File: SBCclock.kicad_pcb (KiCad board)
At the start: 2 copper layers, 37.5 x 23.4 mm, 12 parts, among them J1 Conn_01x06_Male, J2 Conn_01x06_Male, U1 74HCT04, U2 74HC163, U3 74AHC1G02, Y1 25.175MHz

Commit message: chore: tweak values
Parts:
- C2: value 18pF -> 1uF
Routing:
- net Clock6: track 34.2 -> 31.4 mm

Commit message: chore: adjust routing
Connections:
- J2 pad 4: unconnected-(J2-Pin_4-Pad4) -> ~{RESET}
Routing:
- net GND: track 88.7 -> 89.4 mm
- added copper zone on F.Cu, net GND
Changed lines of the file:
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@@
   (net 13 "unconnected-(U1-Pad13)")
   (net 14 "Net-(C1-Pad2)")
-  (net 15 "unconnected-(J2-Pin_4-Pad4)")
+  (net 15 "~{RESET}")
   (net 16 "Net-(U2-CEP)")
   (net 17 "unconnected-(U2-D0-Pad3)")
@@
       (net 9 "~{E}") (pinfunction "Pin_3") (pintype "passive"))
     (pad "4" thru_hole oval (at 0 -7.62 180) (size 1.7 1.7) (drill 1) (layers "*.Cu" "*.Mask")
-      (net 15 "unconnected-(J2-Pin_4-Pad4)") (pinfunction "Pin_4") (pintype "passive+no_connect"))
+      (net 15 "~{RESET}") (pinfunction "Pin_4") (pintype "passive"))
     (pad "5" thru_hole oval (at 0 -10.16 180) (size 1.7 1.7) (drill 1) (layers "*.Cu" "*.Mask")
       (net 6 "Clock3") (pinfunction "Pin_5") (pintype "passive"))
@@
     (style (thickness 0.15) (arrow_length 1.27) (text_position_mode 0) (extension_height 0.58642) (extension_offset 0.5) keep_text_aligned)
   )
+  (dimension (type aligned) (layer "User.2")
+    (pts (xy 143.002 83.3628) (xy 143.002 59.9948))
+    (height -4.4196)
+    (gr_text "23.3680 mm" (at 137.4324 71.6788 90) (layer "User.2")
+      (effects (font (size 1 1) (thickness 0.15)))
+    )
+    (format (prefix "") (suffix "") (units 3) (units_format 1) (precision 4))
+    (style (thickness 0.15) (arrow_length 1.27) (text_position_mode 0) (extension_height 0.58642) (extension_offset 0.5) keep_text_aligned)
+  )
+  (dimension (type aligned) (layer "User.2")
+    (pts (xy 143.002 83.3628) (xy 180.4924 83.3628))
+    (height 3.9116)
+    (gr_text "37.4904 mm" (at 161.7472 86.1244) (layer "User.2")
+      (effects (font (size 1 1) (thickness 0.15)))
+    )
+    (format (prefix "") (suffix "") (units 3) (units_format 1) (precision 4))
+    (style (thickness 0.15) (arrow_length 1.27) (text_position_mode 0) (extension_height 0.58642) (extension_offset 0.5) keep_text_aligned)
+  )
+  (segment (start 156.413 75.7428) (end 156.515 75.7428) (width 0.5) (layer "F.Cu") (net 1))
+  (segment (start 153.304 78.5472) (end 151.9012 78.5472) (width 0.5) (layer "F.Cu") (net 1))
+  (segment (start 177.343 61.3664) (end 167.0812 61.3664) (width 0.5) (layer "F.Cu") (net 1))
+  (segment (start 147.828 63.8048) (end 146.58 63.8048) (width 0.5) (layer "F.Cu") (net 1))
   (segment (start 178.41 68.58) (end 178.41 62.4332) (width 0.5) (layer "F.Cu") (net 1))
-  (segment (start 156.413 75.7428) (end 156.515 75.7428) (width 0.5) (layer "F.Cu") (net 1))
+  (segment (start 178.41 62.4332) (end 177.343 61.3664) (width 0.5) (layer "F.Cu") (net 1))
   (segment (start 156.7688 68.072) (end 159.071 65.7698) (width 0.5) (layer "F.Cu") (net 1))
-  (segment (start 153.304 78.5472) (end 151.9012 78.5472) (width 0.5) (layer "F.Cu") (net 1))
-  (segment (start 147.828 63.8048) (end 146.58 63.8048) (width 0.5) (layer "F.Cu") (net 1))
-  (segment (start 155.956 72.2884) (end 156.7688 71.4756) (width 0.5) (layer "F.Cu") (net 1))
-  (segment (start 168.266 61.3664) (end 166.894 62.738) (width 0.5) (layer "F.Cu") (net 1))
-  (segment (start 177.343 61.3664) (end 168.266 61.3664) (width 0.5) (layer "F.Cu") (net 1))
   (segment (start 155.956 72.2884) (end 155.891 72.2234) (width 0.5) (layer "F.Cu") (net 1))
   (segment (start 156.515 75.7428) (end 156.529 75.757) (width 0.5) (layer "F.Cu") (net 1))
-  (segment (start 178.41 62.4332) (end 177.343 61.3664) (width 0.5) (layer "F.Cu") (net 1))
-  (segment (start 159.071 65.7698) (end 163.8622 65.7698) (width 0.5) (layer "F.Cu") (net 1))
-  (segment (start 163.8622 65.7698) (end 166.894 62.738) (width 0.5) (layer "F.Cu") (net 1))
+  (segment (start 167.0812 61.3664) (end 166.894 61.5536) (width 0.5) (layer "F.Cu") (net 1))
   (segment (start 157.226 75.757) (end 156.602 75.757) (width 0.5) (layer "F.Cu") (net 1))
+  (segment (start 155.956 72.2884) (end 156.7688 71.4756) (width 0.5) (layer "F.Cu") (net 1))
+  (segment (start 166.894 61.5536) (end 166.894 62.738) (width 0.5) (layer "F.Cu") (net 1))
+  (segment (start 159.071 65.7698) (end 162.7794 65.7698) (width 0.5) (layer "F.Cu") (net 1))
   (segment (start 156.7688 71.4756) (end 156.7688 68.072) (width 0.5) (layer "F.Cu") (net 1))
+  (segment (start 165.8112 62.738) (end 166.894 62.738) (width 0.5) (layer "F.Cu") (net 1))
   (segment (start 153.314 78.5368) (end 153.304 78.5472) (width 0.5) (layer "F.Cu") (net 1))
   (segment (start 156.529 75.757) (end 156.602 75.757) (width 0.5) (layer "F.Cu") (net 1))
+  (segment (start 162.7794 65.7698) (end 165.8112 62.738) (width 0.5) (layer "F.Cu") (net 1))
   (segment (start 156.602 75.757) (end 157.226 75.757) (width 0.5) (layer "F.Cu") (net 1))
   (segment (start 155.891 72.2234) (end 154.9146 72.2234) (width 0.5) (layer "F.Cu") (net 1))
@@
     )
   )
-  (zone (net 1) (net_name "GND") (layer "B.Cu") (hatch edge 0.508)
+  (zone (net 1) (net_name "GND") (layers "F&B.Cu") (hatch edge 0.508)
     (connect_pads (clearance 0.508))
     (min_thickness 0.254) (filled_areas_thickness no)

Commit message: revise E generation
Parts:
- added C3: 1uF, Capacitor_SMD:C_0805_2012Metric_Pad1.18x1.45mm_HandSolder, F.Cu at (163.5, 81.1)
- added D1: LED, LED_SMD:LED_0805_2012Metric_Pad1.15x1.40mm_HandSolder, F.Cu at (145.8, 81.0)
- added R5: 330R, Resistor_SMD:R_0805_2012Metric_Pad1.20x1.40mm_HandSolder, F.Cu at (145.8, 78.9)
- added U4: 74AHC1G08, Package_TO_SOT_SMD:SOT-353_SC-70-5_Handsoldering, F.Cu at (156.3, 79.2)
- added U5: 74AHC1G32, Package_TO_SOT_SMD:SOT-353_SC-70-5_Handsoldering, F.Cu at (159.1, 73.9)
- moved U1 9.91 mm to (170.9, 78.6)
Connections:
- U1 pad 1: Net-(C1-Pad2) -> Net-(R3-Pad1)
- U1 pad 2: Net-(R2-Pad2) -> Net-(C1-Pad1)
- U1 pad 3: Net-(R3-Pad1) -> Net-(C1-Pad2)
- U1 pad 4: Net-(C1-Pad1) -> Net-(R2-Pad2)
- U3 pad 4: E -> Net-(U3-Pad4)
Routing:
- net GND: track 89.4 -> 116.7 mm, vias 4 -> 8
- net +5V: track 47.8 -> 72.4 mm
- net Net-(U3-Pad4): track 0.00 -> 11.9 mm
- net Clock24: track 30.3 -> 41.7 mm, vias 1 -> 5
- net Net-(C1-Pad2): track 28.2 -> 39.0 mm, vias 0 -> 2
- net ~{Q}: track 20.0 -> 9.48 mm
- net ~{E}: track 35.1 -> 24.9 mm
- net Net-(U4-Pad4): track 0.00 -> 7.72 mm
- net Net-(R3-Pad1): track 20.8 -> 13.6 mm, vias 2 -> 0
- net Clock3: track 57.5 -> 64.1 mm, vias 2 -> 3
- net E: track 35.6 -> 29.2 mm, vias 0 -> 1
- net Net-(R2-Pad2): track 10.7 -> 16.2 mm
- net Net-(C1-Pad1): track 30.5 -> 25.4 mm, vias 0 -> 3
- net Clock6: track 31.4 -> 34.7 mm
- net Net-(D1-A): track 0.00 -> 2.14 mm

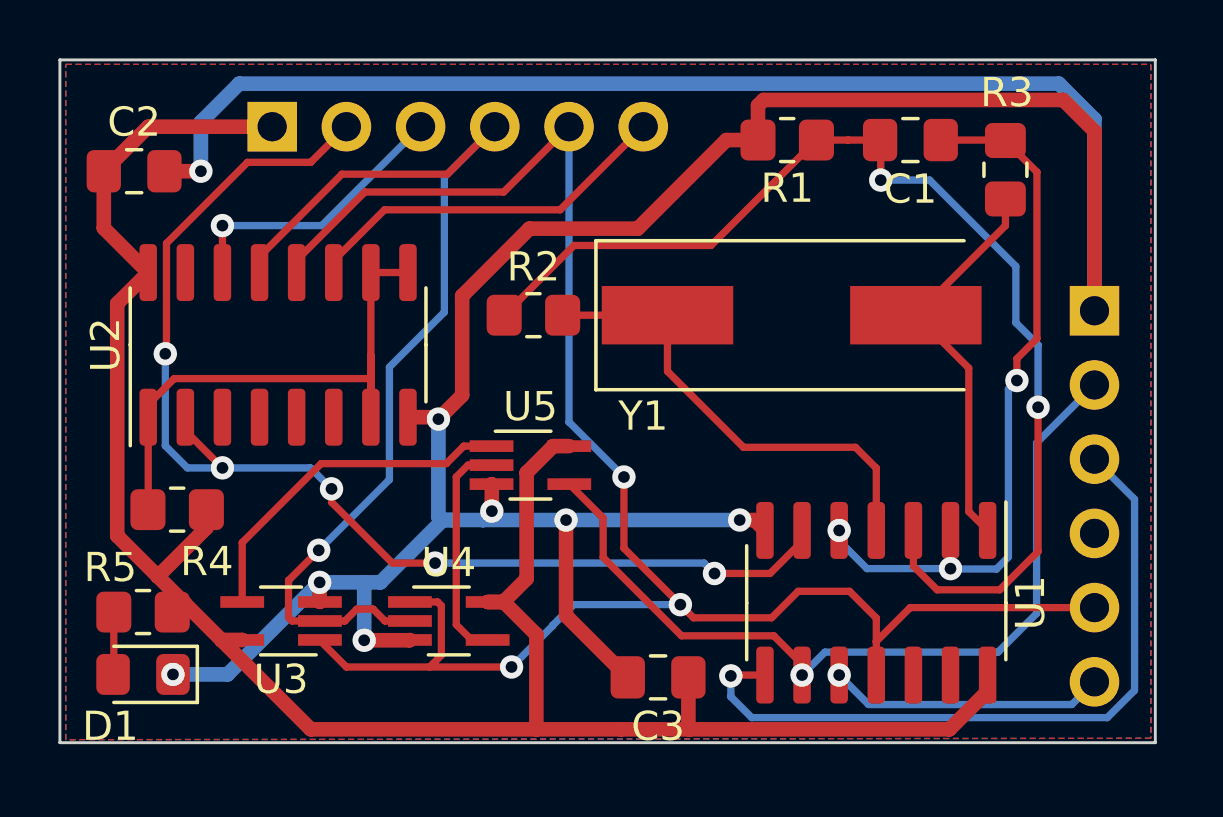
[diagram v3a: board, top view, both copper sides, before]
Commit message: simplified board
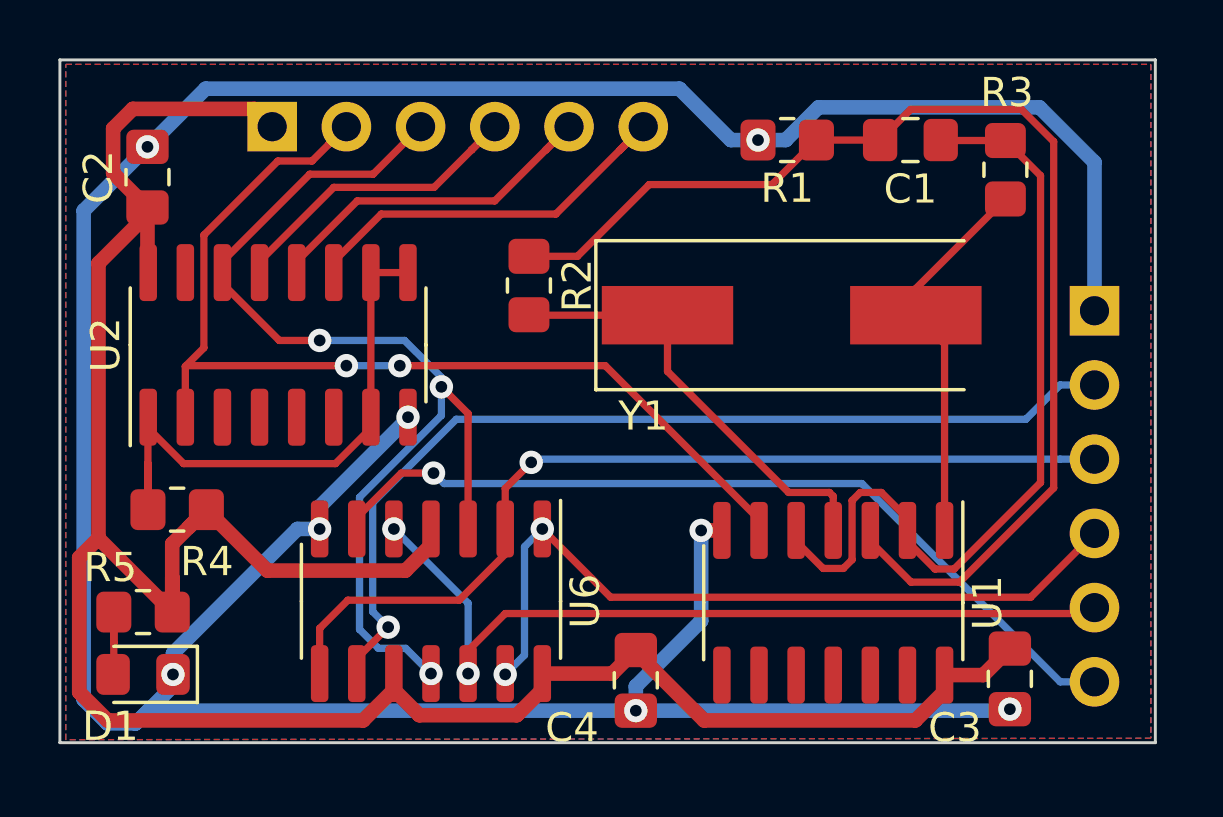
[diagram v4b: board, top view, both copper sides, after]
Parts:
- removed U3: 74AHC1G02, Package_TO_SOT_SMD:SOT-353_SC-70-5_Handsoldering
- removed U4: 74AHC1G08, Package_TO_SOT_SMD:SOT-353_SC-70-5_Handsoldering
- removed U5: 74AHC1G32, Package_TO_SOT_SMD:SOT-353_SC-70-5_Handsoldering
- added C4: 1uF, Capacitor_SMD:C_0805_2012Metric_Pad1.18x1.45mm_HandSolder, F.Cu at (162.7, 81.2)
- added U6: 74HC74, Package_SO:SOIC-14_3.9x8.7mm_P1.27mm, F.Cu at (155.7, 78.5)
- moved C3 12.0 mm to (175.5, 81.2), turned to -90 degrees
- moved U1 1.47 mm to (169.5, 78.6)
- moved R2 1.03 mm to (159.1, 67.7), turned to -90 degrees
- moved C2 0.50 mm to (146.0, 64.0), turned to 90 degrees
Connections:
- J2 pad 5: Clock3 -> Q
- U1 pad 10: ~{Q} -> unconnected-(U1-Pad10)
- U1 pad 11: Clock3 -> unconnected-(U1-Pad11)
- U1 pad 8: ~{E} -> unconnected-(U1-Pad8)
- U1 pad 9: E -> unconnected-(U1-Pad9)
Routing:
- net Clock3: track 64.1 -> 12.9 mm, vias 3 -> 0
- net Q: track 0.00 -> 28.8 mm, vias 0 -> 2
- net Clock12: track 9.79 -> 36.4 mm, vias 1 -> 3
- net ~{RESET}: track 0.00 -> 26.3 mm, vias 0 -> 2
- net Clock6: track 34.7 -> 11.7 mm, vias 1 -> 0
- net ~{Q}: track 9.48 -> 29.2 mm
- net +5V: track 72.4 -> 85.3 mm
- net Net-(U3-Pad4): track 11.9 -> 0.00 mm
- net Net-(U4-Pad4): track 7.72 -> 0.00 mm
- net ~{E}: track 24.9 -> 31.8 mm
- net Clock24: track 41.7 -> 36.1 mm, vias 5 -> 2
- net E: track 29.2 -> 32.9 mm
- net Net-(C1-Pad1): track 25.4 -> 28.7 mm, vias 3 -> 0
- net Net-(C1-Pad2): track 39.0 -> 41.1 mm, vias 2 -> 0
- net GND: track 116.7 -> 114.9 mm
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
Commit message: prepare for production
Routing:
- net +5V: track 85.3 -> 85.9 mm
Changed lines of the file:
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@@
     (fp_line (start 1 0.625) (end -1 0.625)
       (stroke (width 0.1) (type solid)) (layer "F.Fab"))
-    (pad "1" smd roundrect (at -1 0) (size 1.2 1.4) (layers "F.Cu" "F.Paste" "F.Mask") (roundrect_rratio 0.208333)
+    (pad "1" smd roundrect (at -1 0) (size 1.2 1.4) (layers "F.Cu" "F.Paste" "F.Mask") (roundrect_rratio 0.2083333333)
       (net 26 "Net-(D1-A)") (pintype "passive"))
-    (pad "2" smd roundrect (at 1 0) (size 1.2 1.4) (layers "F.Cu" "F.Paste" "F.Mask") (roundrect_rratio 0.208333)
+    (pad "2" smd roundrect (at 1 0) (size 1.2 1.4) (layers "F.Cu" "F.Paste" "F.Mask") (roundrect_rratio 0.2083333333)
       (net 2 "+5V") (pintype "passive"))
     (model "${KICAD6_3DMODEL_DIR}/Resistor_SMD.3dshapes/R_0805_2012Metric.wrl"
@@
     (fp_line (start 1 0.6) (end 1 -0.6)
       (stroke (width 0.1) (type solid)) (layer "F.Fab"))
-    (pad "1" smd roundrect (at -1.025 0 180) (size 1.15 1.4) (layers "F.Cu" "F.Paste" "F.Mask") (roundrect_rratio 0.217391)
+    (pad "1" smd roundrect (at -1.025 0 180) (size 1.15 1.4) (layers "F.Cu" "F.Paste" "F.Mask") (roundrect_rratio 0.2173913043)
       (net 1 "GND") (pinfunction "K") (pintype "passive"))
-    (pad "2" smd roundrect (at 1.025 0 180) (size 1.15 1.4) (layers "F.Cu" "F.Paste" "F.Mask") (roundrect_rratio 0.217391)
+    (pad "2" smd roundrect (at 1.025 0 180) (size 1.15 1.4) (layers "F.Cu" "F.Paste" "F.Mask") (roundrect_rratio 0.2173913043)
       (net 26 "Net-(D1-A)") (pinfunction "A") (pintype "passive"))
     (model "${KICAD6_3DMODEL_DIR}/LED_SMD.3dshapes/LED_0805_2012Metric.wrl"
@@
     (fp_line (start 1 0.625) (end -1 0.625)
       (stroke (width 0.1) (type solid)) (layer "F.Fab"))
-    (pad "1" smd roundrect (at -1.0375 0 270) (size 1.175 1.45) (layers "F.Cu" "F.Paste" "F.Mask") (roundrect_rratio 0.212766)
+    (pad "1" smd roundrect (at -1.0375 0 270) (size 1.175 1.45) (layers "F.Cu" "F.Paste" "F.Mask") (roundrect_rratio 0.2127659574)
       (net 2 "+5V") (pintype "passive"))
-    (pad "2" smd roundrect (at 1.0375 0 270) (size 1.175 1.45) (layers "F.Cu" "F.Paste" "F.Mask") (roundrect_rratio 0.212766)
+    (pad "2" smd roundrect (at 1.0375 0 270) (size 1.175 1.45) (layers "F.Cu" "F.Paste" "F.Mask") (roundrect_rratio 0.2127659574)
       (net 1 "GND") (pintype "passive"))
     (model "${KICAD6_3DMODEL_DIR}/Capacitor_SMD.3dshapes/C_0805_2012Metric.wrl"
@@
     (fp_line (start 1 0.625) (end -1 0.625)
       (stroke (width 0.1) (type solid)) (layer "F.Fab"))
-    (pad "1" smd roundrect (at -1.0375 0 270) (size 1.175 1.45) (layers "F.Cu" "F.Paste" "F.Mask") (roundrect_rratio 0.212766)
+    (pad "1" smd roundrect (at -1.0375 0 270) (size 1.175 1.45) (layers "F.Cu" "F.Paste" "F.Mask") (roundrect_rratio 0.2127659574)
       (net 2 "+5V") (pintype "passive"))
-    (pad "2" smd roundrect (at 1.0375 0 270) (size 1.175 1.45) (layers "F.Cu" "F.Paste" "F.Mask") (roundrect_rratio 0.212766)
+    (pad "2" smd roundrect (at 1.0375 0 270) (size 1.175 1.45) (layers "F.Cu" "F.Paste" "F.Mask") (roundrect_rratio 0.2127659574)
       (net 1 "GND") (pintype "passive"))
     (model "${KICAD6_3DMODEL_DIR}/Capacitor_SMD.3dshapes/C_0805_2012Metric.wrl"
@@
   (segment (start 145.999 65.0455) (end 145.999 65.1617) (width 0.5) (layer "F.Cu") (net 2))
   (segment (start 173.279 81.6019) (end 173.279 81.0484) (width 0.5) (layer "F.Cu") (net 2))
+  (segment (start 143.6624 75.7078) (end 144.323 76.3684) (width 0.5) (layer "F.Cu") (net 2))
   (segment (start 149.657 61.6712) (end 145.496 61.6712) (width 0.5) (layer "F.Cu") (net 2))
   (segment (start 146.0246 67.2734) (end 146.025 67.2734) (width 0.5) (layer "F.Cu") (net 2))
-  (segment (start 145.999 65.278) (end 144.323 66.9544) (width 0.5) (layer "F.Cu") (net 2))
-  (segment (start 144.323 66.9544) (end 144.323 76.3684) (width 0.5) (layer "F.Cu") (net 2))
   (segment (start 162.712 80.264) (end 165.049 82.6008) (width 0.5) (layer "F.Cu") (net 2))
   (segment (start 154.831 77.4726) (end 155.702 76.6011) (width 0.5) (layer "F.Cu") (net 2))
@@
   (segment (start 146.847 77.724) (end 146.847 76.5556) (width 0.5) (layer "F.Cu") (net 2))
   (segment (start 155.702 76.6011) (end 155.702 76.0476) (width 0.5) (layer "F.Cu") (net 2))
+  (segment (start 145.999 65.278) (end 143.6624 67.6146) (width 0.5) (layer "F.Cu") (net 2))
   (segment (start 147.431 75.9714) (end 148.0152 75.3872) (width 0.5) (layer "F.Cu") (net 2))
   (segment (start 153.382 82.6008) (end 154.432 81.5511) (width 0.5) (layer "F.Cu") (net 2))
@@
   (segment (start 150.2664 62.2808) (end 150.266 62.2808) (width 0.5) (layer "F.Cu") (net 2))
   (segment (start 145.999 67.248) (end 146.025 67.2734) (width 0.5) (layer "F.Cu") (net 2))
+  (segment (start 143.6624 67.6146) (end 143.6624 75.7078) (width 0.5) (layer "F.Cu") (net 2))
   (segment (start 145.999 65.1617) (end 145.999 65.278) (width 0.5) (layer "F.Cu") (net 2))
   (segment (start 145.999 65.1617) (end 145.9992 65.1615) (width 0.5) (layer "F.Cu") (net 2))

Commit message: revise clock signal
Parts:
- removed the R3 at (175.4, 63.8)
- added C2: 22pF, Capacitor_SMD:C_0805_2012Metric_Pad1.18x1.45mm_HandSolder, F.Cu at (172.3, 63.7)
- added D2: LED, LED_SMD:LED_0805_2012Metric_Pad1.15x1.40mm_HandSolder, F.Cu at (178.1, 64.8)
- added JP1: SolderJumper_3_Bridged12, Jumper:SolderJumper-3_P1.3mm_Bridged12_Pad1.0x1.5mm, B.Cu at (150.4, 72.5)
- added R5: 330R, Resistor_SMD:R_0805_2012Metric_Pad1.20x1.40mm_HandSolder, F.Cu at (178.3, 61.8)
- C1: value 100pF -> 22pF
- R2: value 1K -> 1M
- U1: value 74HCT04 -> 74HC14
- U2: value 74HC163 -> 74HCT163
- U3: renamed from U6; value 74HC74 -> 74HCT74
- moved R1 8.28 mm to (175.9, 64.9), turned to -90 degrees
- moved C1 5.32 mm to (166.9, 63.7), turned to -90 degrees
- moved R2 0.69 mm to (159.0, 68.4), turned to 180 degrees
- moved Y1 0.36 mm to (168.1, 68.4)
- moved U1 0.08 mm to (169.5, 78.5)
- renumbered C2 to C5, R4 to R3, R5 to R4
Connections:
- C1 pad 1: Net-(C1-Pad1) -> GND
- R1 pad 1: Net-(C1-Pad2) -> Net-(C2-Pad2)
- R1 pad 2: GND -> Net-(R1-Pad2)
- R2 pad 2: Net-(R2-Pad2) -> Net-(R1-Pad2)
- U1 pad 1: Net-(R3-Pad1) -> Net-(C1-Pad2)
- U1 pad 10: unconnected-(U1-Pad10) -> RESET
- U1 pad 11: unconnected-(U1-Pad11) -> ~{RESET}
- U1 pad 2: Net-(C1-Pad1) -> Net-(R1-Pad2)
- U1 pad 3: Net-(C1-Pad2) -> Net-(R1-Pad2)
- U1 pad 4: Net-(R2-Pad2) -> Clock24
- U1 pad 5: Net-(C1-Pad1) -> unconnected-(U1-Pad5)
- U1 pad 6: Clock24 -> unconnected-(U1-Pad6)
- U1 pad 8: unconnected-(U1-Pad8) -> Net-(U3A-~{R})
- U1 pad 9: unconnected-(U1-Pad9) -> RESET
- U3 pad 1: ~{RESET} -> Net-(U3A-~{R})
- U3 pad 11: Clock12 -> QuadC
- U3 pad 13: ~{RESET} -> Net-(U3A-~{R})
- U3 pad 3: Clock12 -> QuadC
- Y1 pad 1: Net-(R2-Pad2) -> Net-(C1-Pad2)
- Y1 pad 2: Net-(R3-Pad1) -> Net-(C2-Pad2)
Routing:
- net Net-(R1-Pad2): track 0.00 -> 37.4 mm
- net QuadC: track 0.00 -> 29.1 mm, vias 0 -> 2
- net Net-(C1-Pad1): track 28.7 -> 0.00 mm
- net RESET: track 0.00 -> 28.2 mm, vias 0 -> 2
- net Clock12: track 36.4 -> 16.6 mm, vias 3 -> 1
- net Net-(R2-Pad2): track 15.9 -> 0.00 mm
- net Net-(C1-Pad2): track 41.1 -> 25.9 mm
- net Net-(U3A-~{R}): track 0.00 -> 14.8 mm, vias 0 -> 2
- net Net-(R3-Pad1): track 13.6 -> 0.00 mm
- net ~{RESET}: track 26.3 -> 15.3 mm, vias 2 -> 0
- net Net-(C2-Pad2): track 0.00 -> 8.47 mm
- net Clock6: track 11.7 -> 17.2 mm, vias 0 -> 1
- net GND: track 114.9 -> 117.8 mm, vias 8 -> 9
- net Clock24: track 36.1 -> 38.5 mm
- net Net-(D2-A): track 0.00 -> 2.32 mm
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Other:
- board text added: "/2"
- board text added: "/4"
- board text added: "Quadrature Input"

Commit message: v2 board
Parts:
- removed JP1: SolderJumper_3_Bridged12, Jumper:SolderJumper-3_P1.3mm_Bridged12_Pad1.0x1.5mm
- added C6: 1uF, Capacitor_SMD:C_0805_2012Metric_Pad1.18x1.45mm_HandSolder, B.Cu at (171.7, 78.5)
- added U5: 74HCT153, Package_SO:SOIC-16_3.9x9.9mm_P1.27mm, F.Cu at (167.2, 78.6)
- C1, C3, C4, C5, R2, R3, R4, R5: moved to B.Cu
- J1, J2: value Conn_01x06_Male -> Conn_01x07; footprint Connector_PinHeader_2.54mm:PinHeader_1x06_P2.54mm_Vertical -> Connector_PinHeader_2.54mm:PinHeader_1x07_P2.54mm_Vertical
- U1: value 74HC14 -> 74HCT14
- U3: value 74HCT74 -> 74HCT112; footprint Package_SO:SOIC-14_3.9x8.7mm_P1.27mm -> Package_SO:SOIC-16_3.9x9.9mm_P1.27mm
- moved C3 32.7 mm to (146.8, 65.5), turned to 0 degrees
- moved D1 29.0 mm to (167.2, 61.5)
- moved R4 27.6 mm to (167.2, 61.5)
- moved R1 27.1 mm to (150.7, 74.8), turned to 180 degrees
- moved C4 23.9 mm to (177.3, 62.3), turned to 90 degrees
- moved C1 22.9 mm to (146.8, 74.8), turned to 180 degrees
- moved U1 21.7 mm to (149.6, 69.8), turned to 90 degrees
- moved Y1 19.9 mm to (151.0, 78.7)
- moved U3 19.6 mm to (172.3, 68.0), turned to 0 degrees
- moved C2 19.0 mm to (159.5, 77.6)
- moved R3 14.7 mm to (160.6, 69.8), turned to 0 degrees
- moved R2 12.2 mm to (146.9, 69.9), turned to 0 degrees
- moved C5 11.6 mm to (157.5, 65.4), turned to 0 degrees
- moved U2 10.4 mm to (160.9, 69.8)
- moved D2 5.83 mm to (173.3, 61.5), turned to 0 degrees
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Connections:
- J1 pad 1: +5V -> SEL0
- J1 pad 2: Clock24 -> SEL1
- J1 pad 3: Clock12 -> Clock24
- J1 pad 4: Clock6 -> Clock12
- J1 pad 5: Clock3 -> Clock6
- J1 pad 6: Clock1.5 -> Clock3
- U1 pad 12: unconnected-(U1-Pad12) -> E
- U1 pad 13: unconnected-(U1-Pad13) -> ~{E}
- U1 pad 5: unconnected-(U1-Pad5) -> ~{Q}
- U1 pad 6: unconnected-(U1-Pad6) -> Q
- U3 pad 1: Net-(U3A-~{R}) -> QuadC
- U3 pad 11: QuadC -> Net-(U3A-Q)
- U3 pad 12: Q -> ~{Q}
- U3 pad 13: Net-(U3A-~{R}) -> QuadC
- U3 pad 14: +5V -> Net-(U3A-~{R})
- U3 pad 2: ~{E} -> Net-(U3A-K)
- U3 pad 3: QuadC -> ~{E}
- U3 pad 5: Q -> Net-(U3A-Q)
- U3 pad 7: GND -> ~{E}
- U3 pad 8: ~{E} -> GND
- U3 pad 9: E -> Net-(U3A-K)
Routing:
- net GND: track 117.8 -> 5.92 mm, vias 9 -> 10
- net +5V: track 85.9 -> 11.9 mm, vias 0 -> 8
- net SEL1: track 0.00 -> 53.1 mm
- net SEL0: track 0.00 -> 48.1 mm
- net Net-(R1-Pad2): track 37.4 -> 6.92 mm, vias 0 -> 1
- net ~{RESET}: track 15.3 -> 41.4 mm, vias 0 -> 2
- net ~{Q}: track 29.5 -> 52.8 mm
- net Clock24: track 38.5 -> 20.9 mm, vias 2 -> 0
- net Net-(C1-Pad2): track 25.9 -> 9.32 mm, vias 0 -> 2
- net Net-(U3A-K): track 0.00 -> 16.0 mm, vias 0 -> 2
- net ~{E}: track 32.6 -> 46.1 mm, vias 1 -> 2
- net Net-(U3A-Q): track 0.00 -> 9.56 mm
- net Net-(U3A-~{R}): track 14.8 -> 24.0 mm
- net E: track 32.4 -> 40.3 mm
- net Clock3: track 12.9 -> 18.6 mm
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- added copper zone on In2.Cu, net +5V
- added copper zone on In1.Cu, net GND
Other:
- copper layers 2 -> 4
- board text removed: "/2"
- board text removed: "/4"
- board text removed: "Quadrature Input"
